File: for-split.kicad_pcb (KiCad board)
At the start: 2 copper layers, 114.3 x 95.3 mm, 73 parts, among them J1 TRRS, J2 TRRS, U1 ProMicro

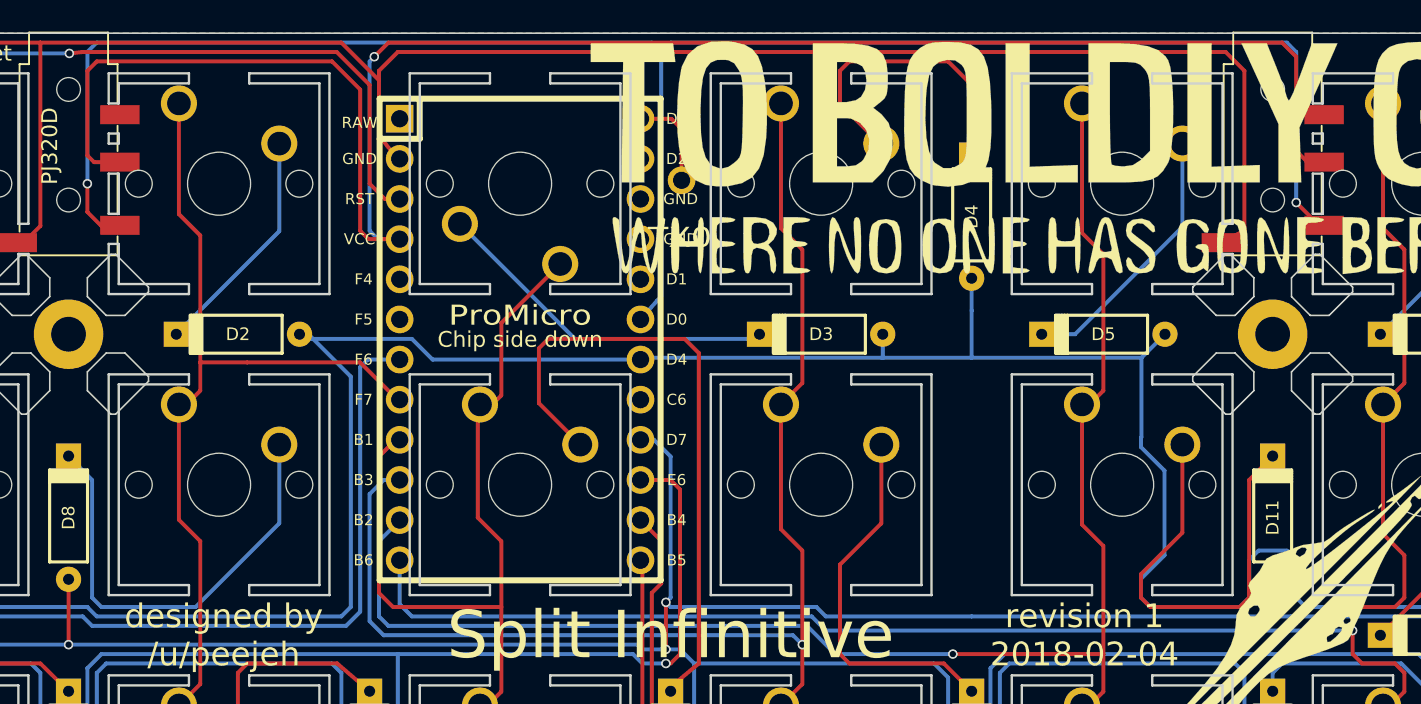
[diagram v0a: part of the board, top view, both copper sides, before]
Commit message: Add extradata pad and connection
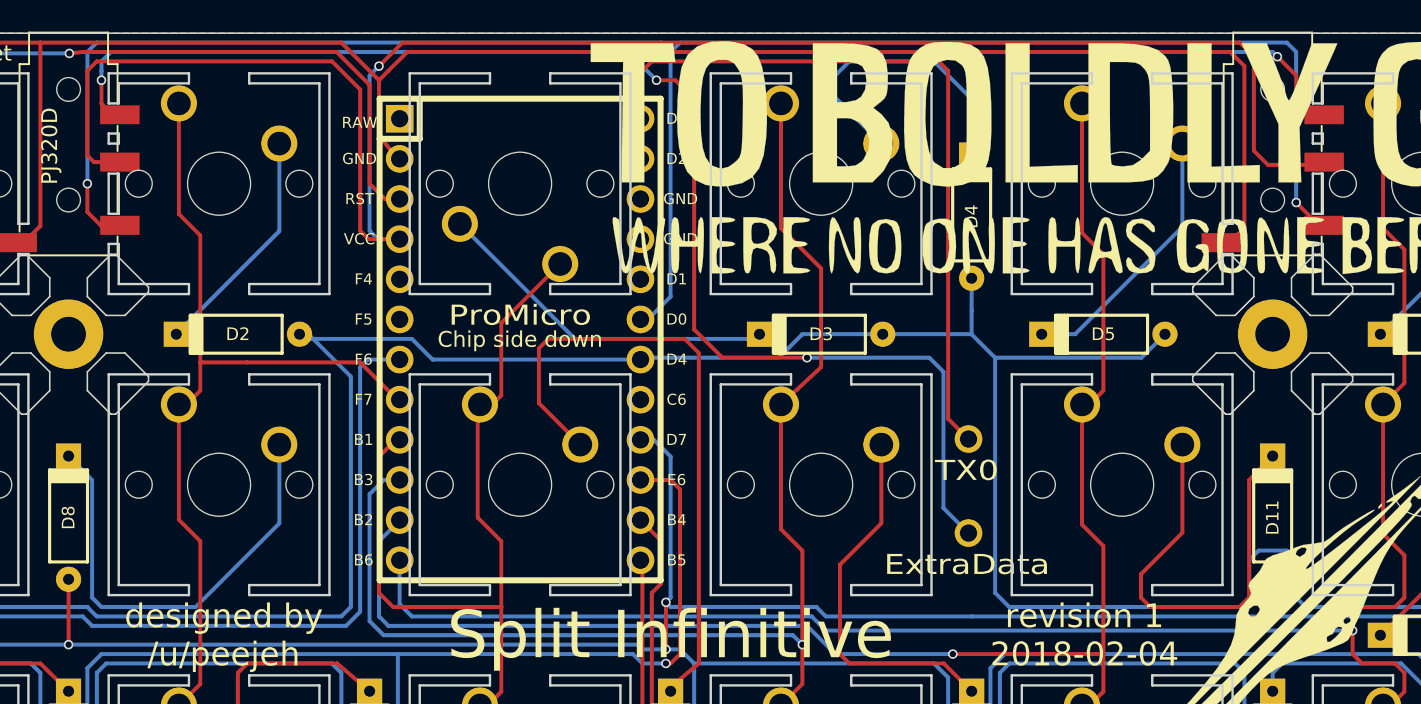
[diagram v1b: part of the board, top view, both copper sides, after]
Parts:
- added EXTRADATA1: ExtraData, canadian_footprints:SIngle_Pad, F.Cu at (183.1, 97.9)
- moved TX0 24.4 mm to (183.1, 92.0)
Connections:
- J1 pad 3: Net-(J1-Pad3) -> Net-(EXTRADATA1-Pad1)
- J2 pad 3: Net-(J2-Pad3) -> Net-(EXTRADATA1-Pad1)
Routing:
- net Net-(EXTRADATA1-Pad1): track 0.00 -> 130.3 mm, vias 0 -> 5
- net Net-(TX0-Pad1): track 6.11 -> 46.8 mm
- net /Row0: track 194.4 -> 200.4 mm
- net /Col3: track 126.8 -> 127.8 mm
- net VCC: track 119.2 -> 118.6 mm

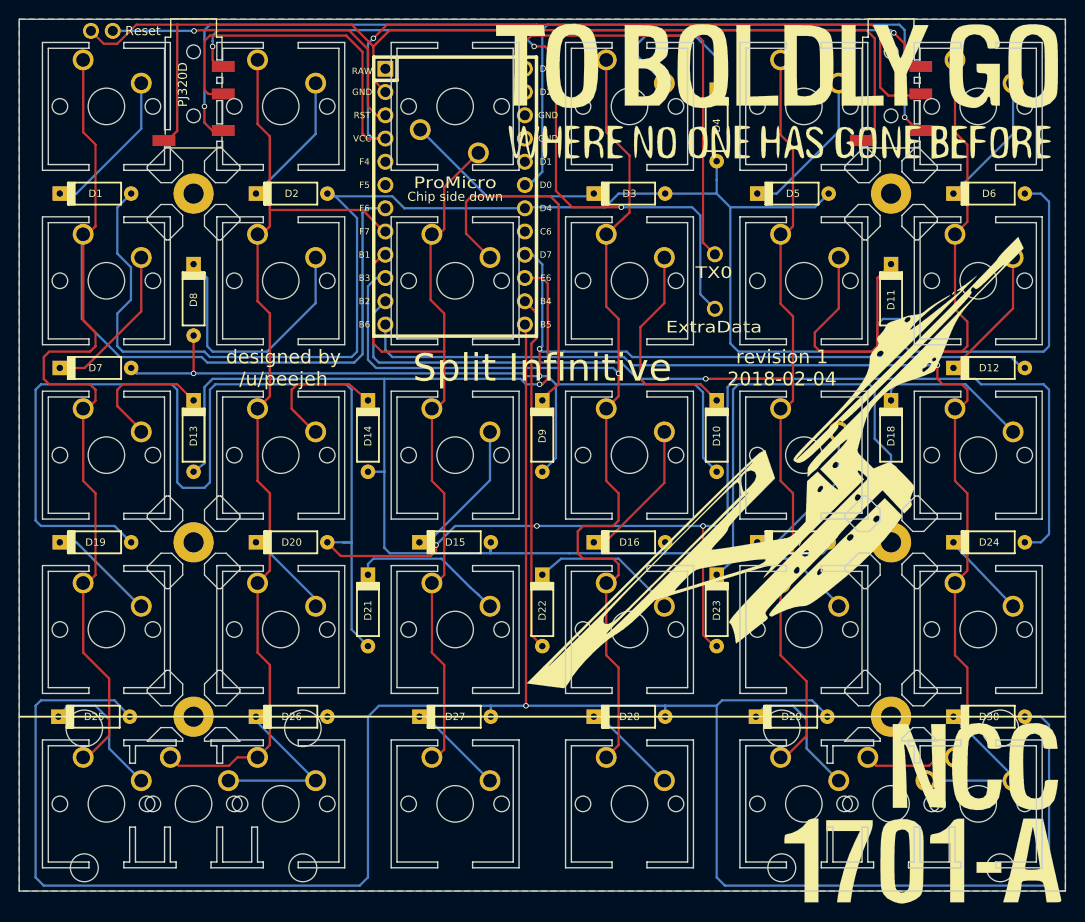
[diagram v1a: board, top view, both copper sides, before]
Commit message: Add routes for indicator LEDs
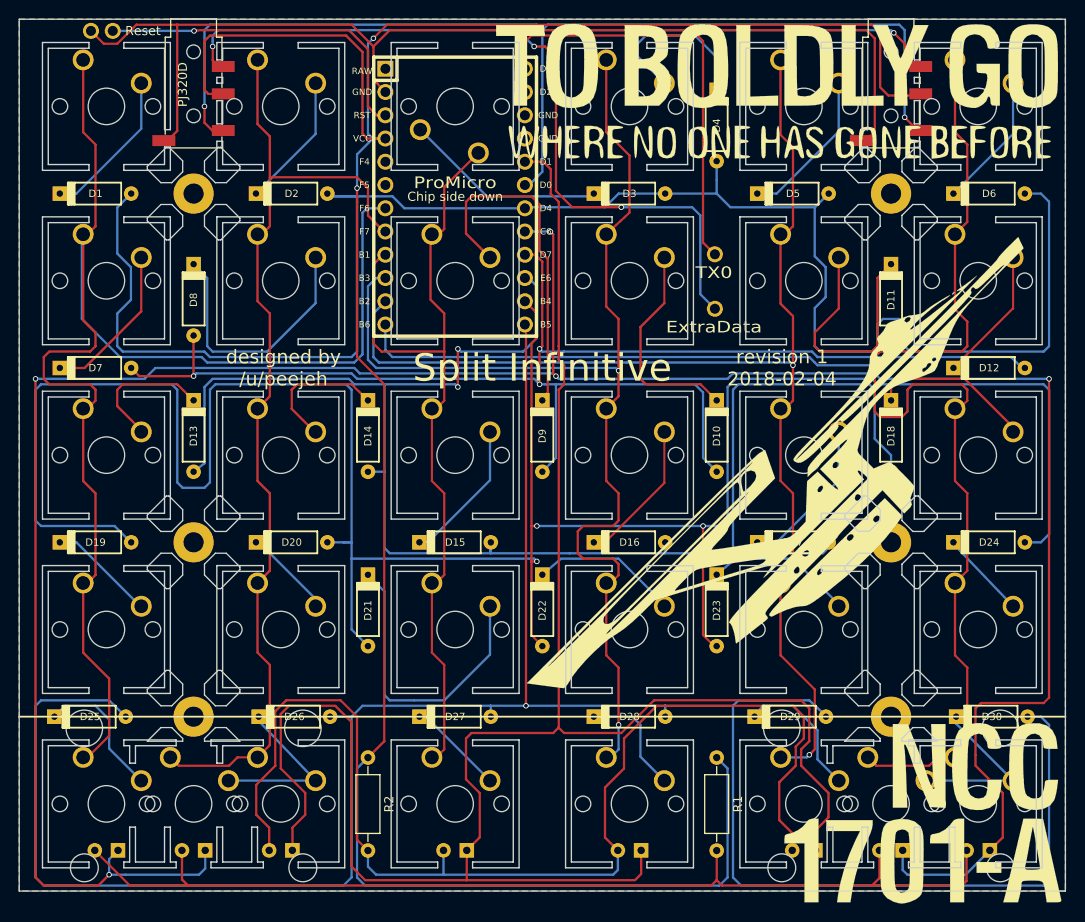
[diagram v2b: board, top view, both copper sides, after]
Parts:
- added L1:0: LED, idle-hands:MX_LED, B.Cu at (211.9, 150.0)
- added L1:1: LED, idle-hands:MX_LED, B.Cu at (202.4, 150.0)
- added L1:2: LED, idle-hands:MX_LED, B.Cu at (116.7, 150.0)
- added L1:3: LED, idle-hands:MX_LED, B.Cu at (126.2, 150.0)
- added L2:0: LED, idle-hands:MX_LED, B.Cu at (192.9, 150.0)
- added L2:1: LED, idle-hands:MX_LED, B.Cu at (173.8, 150.0)
- added L2:2: LED, idle-hands:MX_LED, B.Cu at (135.7, 150.0)
- added L2:3: LED, idle-hands:MX_LED, B.Cu at (154.8, 150.0)
- added R1: R, Resistors_THT:R_Axial_DIN0207_L6.3mm_D2.5mm_P10.16mm_Horizontal, F.Cu at (183.4, 145.0)
- added R2: R, Resistors_THT:R_Axial_DIN0207_L6.3mm_D2.5mm_P10.16mm_Horizontal, F.Cu at (145.3, 145.0)
- moved D25 0.45 mm to (114.9, 140.5)
- moved D30 0.30 mm to (213.4, 140.5)
- moved D26 0.30 mm to (137.2, 140.5)
- moved D29 0.15 mm to (191.4, 140.5)
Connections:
- U1 pad 17: Net-(U1-Pad17) -> /LED2
- U1 pad 20: Net-(U1-Pad20) -> /LED1
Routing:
- net /LED1: track 0.00 -> 283.9 mm, vias 0 -> 5
- net /LED2: track 0.00 -> 215.9 mm
- net VCC: track 118.6 -> 257.4 mm, vias 1 -> 2
- net Net-(L2:0-Pad2): track 0.00 -> 128.0 mm
- net Net-(L1:0-Pad2): track 0.00 -> 112.4 mm
- net Net-(D21-Pad1): track 16.9 -> 33.0 mm
- net /Col5: track 160.2 -> 173.5 mm
- net /Row0: track 200.4 -> 193.8 mm
- net /Row4: track 260.8 -> 256.0 mm
- net /Row3: track 283.4 -> 279.1 mm
- net /Col1: track 104.8 -> 108.0 mm
- net /Row2: track 179.6 -> 176.8 mm, vias 1 -> 2
- net Net-(D28-Pad1): track 10.7 -> 13.4 mm
- net Net-(D9-Pad1): track 40.2 -> 37.8 mm
- net /Col4: track 136.5 -> 138.3 mm, vias 1 -> 2
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
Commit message: Increase size of switch cutouts
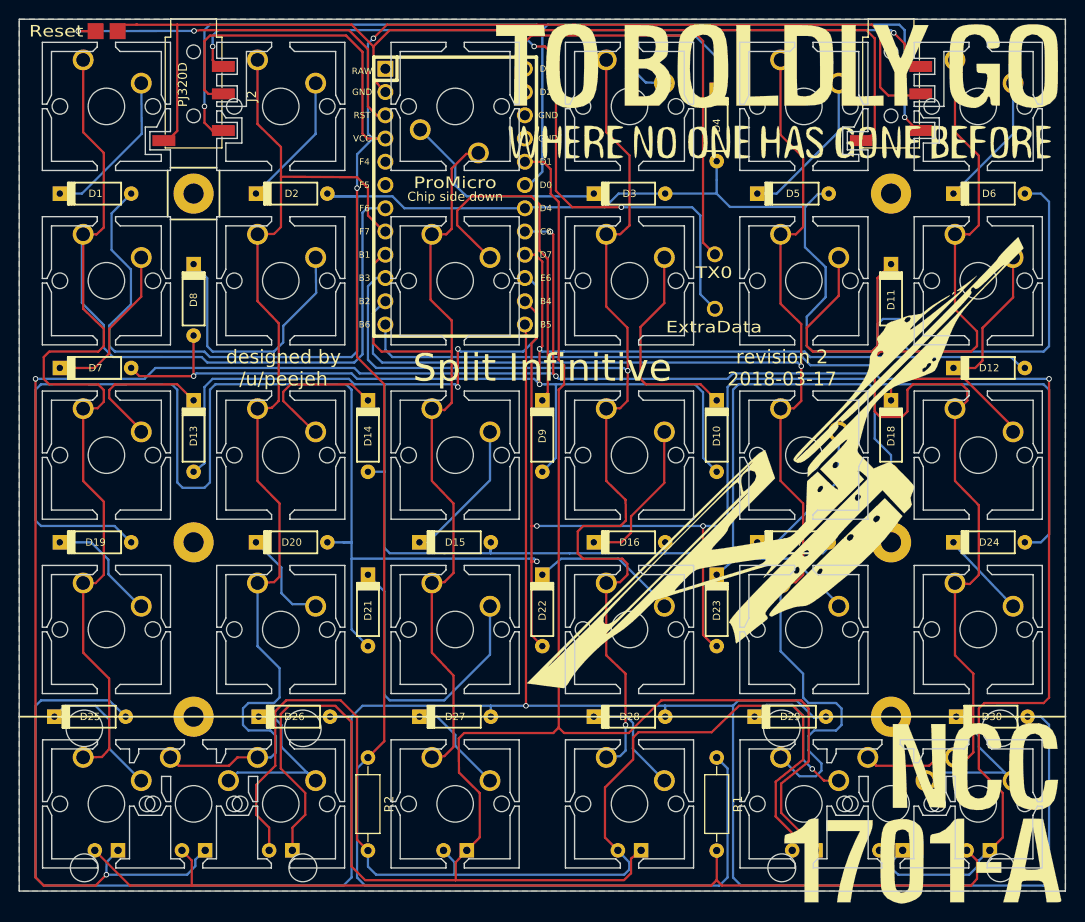
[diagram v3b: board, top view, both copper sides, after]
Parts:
- MX0:0, MX0:4: footprint idle-hands:MX_CUTOUT_VERT_PAD1 -> idle-hands:MX_CUTOUT_PAD1
- MX0:1, MX0:5: footprint idle-hands:MX_CUTOUT_VERT_PAD3 -> idle-hands:MX_CUTOUT_PAD3
- MX0:2, MX0:3, MX1:0, MX1:1, MX1:2, MX1:3, MX1:4, MX1:5, MX2:0, MX2:1, MX2:2, MX2:3, MX2:4, MX2:5, MX3:0, MX3:1, MX3:2, MX3:3, MX3:4, MX3:5, MX4:2, MX4:3: footprint idle-hands:MX_CUTOUT_VERT -> idle-hands:MX_CUTOUT
- MX4:1, MX4:5: footprint idle-hands:MX2U_CUTOUT_VERT -> idle-hands:MX2U_CUTOUT
- moved GROUND1 2.90 mm to (117.8, 67.6)
- moved RESET1 1.88 mm to (115.4, 67.6)
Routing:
- net /Col4: track 138.3 -> 153.6 mm, vias 2 -> 1
- net /Col1: track 108.0 -> 119.8 mm
- net /Col3: track 128.0 -> 135.6 mm
- net /Col0: track 153.4 -> 160.5 mm
- net /Col5: track 173.5 -> 180.5 mm
- net /Col2: track 91.3 -> 97.1 mm
- net Net-(RESET1-Pad1): track 37.3 -> 43.0 mm, vias 1 -> 2
- net GND: track 120.8 -> 116.8 mm
- net /Row0: track 193.8 -> 197.2 mm
- net Net-(D4-Pad1): track 19.0 -> 21.3 mm
- net Net-(D26-Pad1): track 19.1 -> 21.3 mm
- net Net-(L1:0-Pad2): track 112.4 -> 114.5 mm
- net Net-(L2:0-Pad2): track 128.0 -> 130.1 mm
- net /LED2: track 215.9 -> 217.5 mm
- net Net-(D12-Pad1): track 14.8 -> 16.2 mm
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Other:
- outline, holes or cut-outs redrawn
- board text added: "revision 2 2018-03-17"
- board text removed: "revision 1 2018-02-04"
